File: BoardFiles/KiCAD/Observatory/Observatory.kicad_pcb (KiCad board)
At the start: 4 copper layers, 213.4 x 79.7 mm, 63 parts, among them J1 JScope V+, J10 Dio_Jump, J11 nRF Connections, J12 Sulu Header, J13 Serial, J14 RsTx_Dio, J15 RsRx_Dio, J16 JScope Voltage, J17 WaveGen. 1 Mux Config., J2 Analog Discovery Connection, J20 Mounting Hole, J21 Mounting Hole, J22 Mounting Hole, J23 Mounting Hole, J24 prog. LED, J25 JScope V-, J26 Jumper, J27 Jumper, J28 Jumper, J29 Jumper, J3 Digitial Discovery Connection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, J30 Conn_Coaxial_Small, J31 Jumper, J32 Jumper, J33 Conn_Coaxial_Small, J34 JScope I+, J35 JScope I-, J4 Scope 1 Mux Config., J5 Scope 2 Mux Config., J8 JScope Current IO, J9 5V_in, Q2 2N7002, SW1 SW_DIP_x08, SW2 SW_DIP_x08, U1 1, U2 Scope 1 Mux, U3 Wave Gen. Mux, U4 Scope 2 Mux, U5 Pico

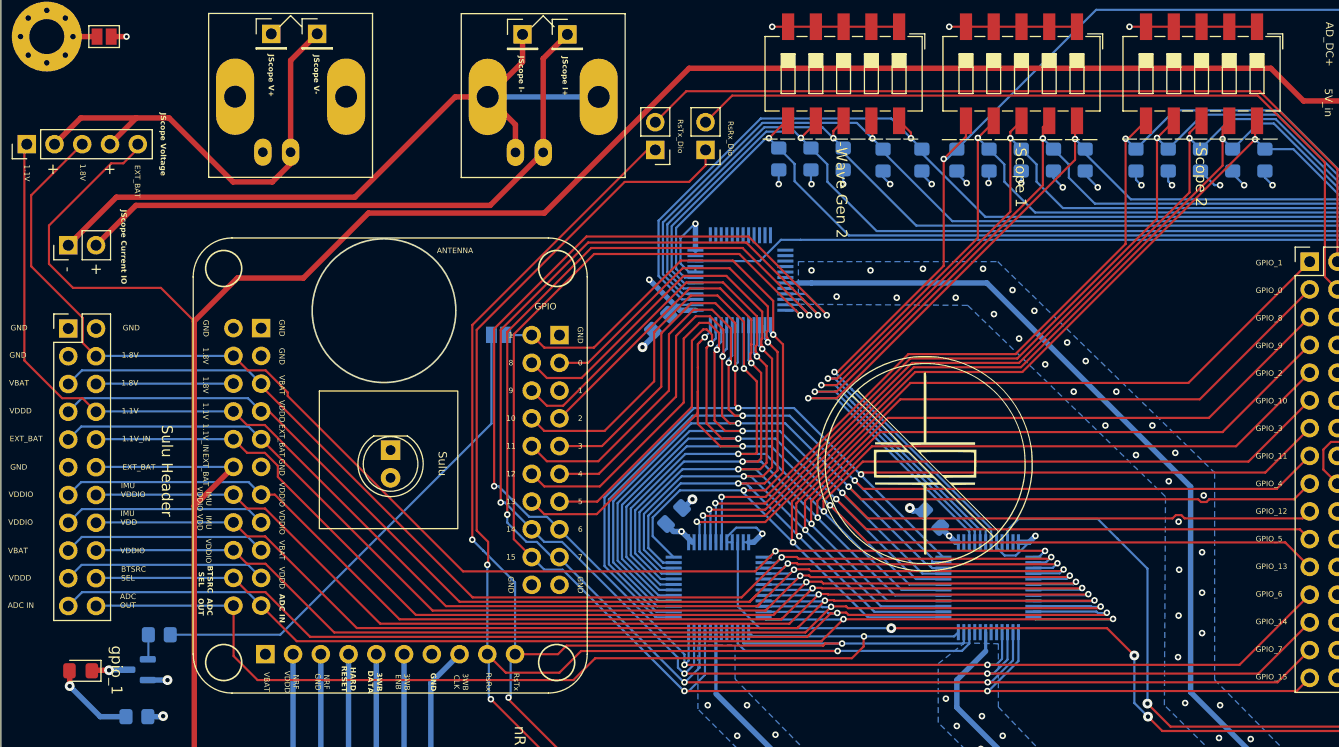
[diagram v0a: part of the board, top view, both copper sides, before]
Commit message: LED circuit fix, added decoupling cap
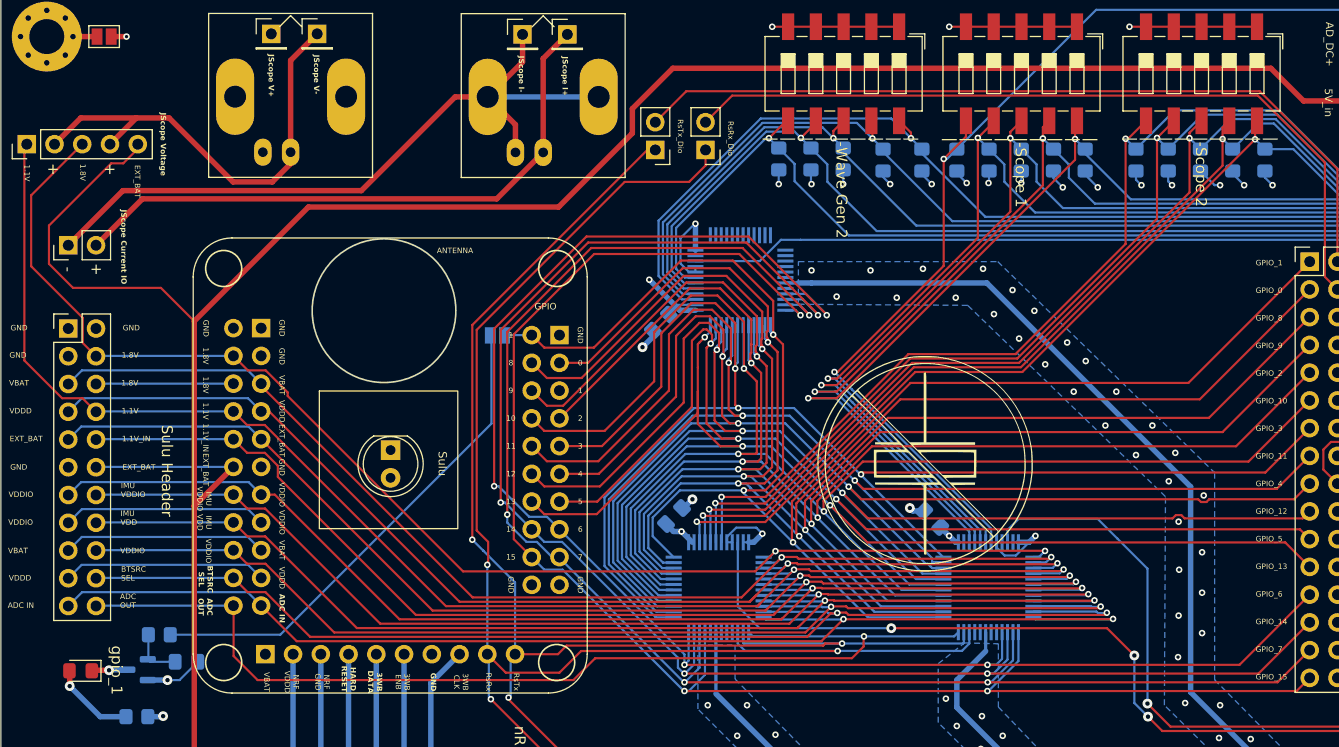
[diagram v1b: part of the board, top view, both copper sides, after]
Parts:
- added C1: 10n, Capacitor_SMD:C_0805_2012Metric_Pad1.18x1.45mm_HandSolder, B.Cu at (58.2, 96.1)
- moved J32 0.11 mm to (86.7, 66.2)
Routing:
- net AD_Scope1-: track 91.8 -> 95.3 mm
- net Net-(Q2-G): track 2.27 -> 4.86 mm
- net Net-(J12-Pin_12): track 209.9 -> 211.2 mm
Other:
- board text added: "WEST LAB CAPSTONE SCUM OBSERVATORY REV2.1"
- board text removed: "WEST LAB CAPSTONE SCUM OBSERVATORY REV2"

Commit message: REV3 begin
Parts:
- removed SW1, SW2: SW_DIP_x08, Button_Switch_SMD:SW_DIP_SPSTx08_Slide_6.7x21.88mm_W8.61mm_P2.54mm_LowProfile
- J11: footprint Connector_PinHeader_2.54mm:PinHeader_1x06_P2.54mm_Vertical -> Connector_PinHeader_2.54mm:PinHeader_1x06_P2.54mm_Horizontal
- J12: value Sulu Header -> Sulu J1 Header
- J13, J9: footprint Connector_PinHeader_2.54mm:PinHeader_1x02_P2.54mm_Vertical -> Connector_PinHeader_2.54mm:PinHeader_1x02_P2.54mm_Horizontal
- J16: value JScope Voltage -> JScope V Ref
- J17, J4, J5: moved to B.Cu
- J24: footprint Connector_PinHeader_2.54mm:PinHeader_1x03_P2.54mm_Vertical -> Button_Switch_THT:SW_CK_JS202011CQN_DPDT_Straight
- J3: value Digitial Discovery Connection Center -> Digitial Discovery Connection
- J31: moved to F.Cu
- J8: value JScope Current IO -> JScope I Loop
- moved J14 181.1 mm to (278.4, 85.7)
- moved J15 179.0 mm to (280.4, 88.1)
- moved J22 177.2 mm to (176.7, -50.3)
- moved J28 174.8 mm to (182.8, -52.5)
- moved J17 154.4 mm to (270.6, 68.1)
- moved J2 138.5 mm to (112.3, 116.6), turned to -90 degrees
- moved J5 136.4 mm to (270.6, 53.5)
- moved J4 119.5 mm to (270.6, 38.4)
- moved J23 109.6 mm to (176.7, -42.4)
- moved J29 107.5 mm to (182.8, -49.0), turned to 0 degrees
- moved J31 99.6 mm to (180.3, -58.0)
- moved R2 95.7 mm to (214.0, 127.0)
- moved R3 95.1 mm to (210.0, 127.0)
- moved R4 94.5 mm to (206.0, 127.0)
- moved R5 93.9 mm to (202.0, 127.0)
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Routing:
- net Net-(J12-Pin_12): track 211.2 -> 13.0 mm
- net WaveGen. Mux Control 4: track 185.5 -> 5.84 mm, vias 1 -> 0
- net WaveGen. Mux Control 3: track 183.4 -> 6.72 mm, vias 1 -> 0
- net AD_Scope2+: track 226.3 -> 52.0 mm
- net WaveGen. Mux Control 2: track 180.5 -> 7.59 mm, vias 1 -> 0
- net Scope 2 Mux ~EN: track 153.4 -> 9.80 mm, vias 2 -> 0
- net Scope 1 Mux ~EN: track 178.8 -> 40.5 mm, vias 4 -> 1
- net Scope 2 Mux Control 4: track 168.4 -> 35.6 mm, vias 2 -> 1
- net WaveGen. 1 Mux ~EN: track 125.8 -> 10.4 mm, vias 2 -> 0
- net AD_Scope1+: track 187.9 -> 73.4 mm
- net WaveGen. Mux Control 1: track 178.0 -> 66.7 mm, vias 1 -> 0
- net Scope 2 Mux Control 3: track 151.5 -> 40.4 mm, vias 2 -> 1
- net WaveGen. Mux Control 0: track 173.9 -> 66.9 mm, vias 1 -> 0
- net Scope 2 Mux Control 2: track 148.4 -> 45.0 mm, vias 2 -> 1
- net Scope 1 Mux Control 1: track 132.9 -> 37.3 mm, vias 2 -> 1
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- removed copper zone on B.Cu, net AD_Scope1-
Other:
- board size 213.4 x 79.7 mm -> 182.1 x 80.6 mm
- board text added: "Current"
- board text added: "Observatory Power V+ Select"
- board text added: "On"
- board text added: "Voltage"
- board text removed: "AD0"
- board text removed: "AD1"
- board text removed: "AD10"
- board text removed: "AD11"
- board text removed: "AD12"
- board text removed: "AD13"
- board text removed: "AD14"
- board text removed: "AD15"
- board text removed: "AD2"
- board text removed: "AD3"
- board text removed: "AD4"
- board text removed: "AD5"
- board text removed: "AD6"
- board text removed: "AD7"
- board text removed: "AD8"
- board text removed: "AD9"
- board text removed: "ADio_Jump"
- board text removed: "Observatory V+"
- board text removed: "Observatory V+ Select"
- board text removed: "V_sys to observatory supply"
- board text removed: "WEST LAB CAPSTONE SCUM OBSERVATORY REV2.1"

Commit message: REV3 begin
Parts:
- removed J14: RsTx_Dio, Connector_PinHeader_2.54mm:PinHeader_1x02_P2.54mm_Vertical
- removed J15: RsRx_Dio, Connector_PinHeader_2.54mm:PinHeader_1x02_P2.54mm_Vertical
- J12: value Sulu J1 Header -> Sulu Header
- J16: value JScope V Ref -> JScope Voltage
- J3: value Digitial Discovery Connection -> Digitial Discovery Connection Center
- J8: value JScope I Loop -> JScope Current IO
- moved J22 121.9 mm to (87.1, 32.4)
- moved J23 121.9 mm to (87.1, 40.3)
- moved J28 121.9 mm to (93.2, 30.2)
- moved J29 121.9 mm to (93.2, 33.7)
- moved J31 121.9 mm to (90.7, 24.7)
- moved J16 16.5 mm to (68.5, 62.9), turned to 90 degrees
- moved J11 7.01 mm to (160.2, 135.4)
- moved J13 7.01 mm to (170.0, 135.4)
- moved J9 7.01 mm to (139.0, 135.4)
- moved U5 6.65 mm to (239.4, 112.5)
- moved C5 2.95 mm to (145.0, 70.8)
- moved U3 2.95 mm to (152.3, 66.9)
- moved J25 2.80 mm to (68.1, 97.4)
- moved J1 2.80 mm to (68.1, 93.2)
- moved J30 2.80 mm to (79.0, 75.6)
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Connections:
- J10 pad 2: DD_DIN_0 -> DD_DIN_1
- J10 pad 4: DD_DIN_1 -> DD_DIN_0
- U5 pad 1: unconnected-(U5-GPIO0-Pad1) -> Scope 1 Mux Control 0
- U5 pad 10: Scope 2 Mux ~EN -> Scope 2 Mux Control 2
- U5 pad 11: WaveGen. 1 Mux ~EN -> Scope 2 Mux Control 3
- U5 pad 2: unconnected-(U5-GPIO1-Pad2) -> Scope 1 Mux Control 1
- U5 pad 21: Scope 2 Mux Control 3 -> unconnected-(U5-GPIO16-Pad21)
- U5 pad 22: Scope 2 Mux Control 2 -> unconnected-(U5-GPIO17-Pad22)
- U5 pad 24: Scope 2 Mux Control 1 -> unconnected-(U5-GPIO18-Pad24)
- U5 pad 25: Scope 2 Mux Control 0 -> unconnected-(U5-GPIO19-Pad25)
- U5 pad 26: Scope 1 Mux Control 0 -> unconnected-(U5-GPIO20-Pad26)
- U5 pad 27: Scope 1 Mux Control 1 -> unconnected-(U5-GPIO21-Pad27)
- U5 pad 29: Scope 1 Mux Control 2 -> unconnected-(U5-GPIO22-Pad29)
- U5 pad 31: Scope 1 Mux Control 3 -> unconnected-(U5-GPIO26_ADC0-Pad31)
- U5 pad 32: Scope 1 Mux Control 4 -> unconnected-(U5-GPIO27_ADC1-Pad32)
- U5 pad 4: unconnected-(U5-GPIO2-Pad4) -> Scope 1 Mux Control 2
- U5 pad 5: unconnected-(U5-GPIO3-Pad5) -> Scope 1 Mux Control 3
- U5 pad 6: unconnected-(U5-GPIO4-Pad6) -> Scope 1 Mux Control 4
- U5 pad 7: unconnected-(U5-GPIO5-Pad7) -> Scope 2 Mux Control 0
- U5 pad 9: Scope 1 Mux ~EN -> Scope 2 Mux Control 1
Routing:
- net Scope 1 Mux Control 0: track 37.5 -> 152.7 mm, vias 1 -> 2
- net Scope 1 Mux Control 1: track 37.3 -> 151.6 mm, vias 1 -> 2
- net WaveGen. Mux Control 4: track 5.84 -> 116.2 mm
- net Scope 1 Mux Control 2: track 37.0 -> 147.0 mm, vias 1 -> 2
- net WaveGen. Mux Control 3: track 6.72 -> 115.5 mm
- net WaveGen. Mux Control 2: track 7.59 -> 115.8 mm
- net Scope 1 Mux Control 3: track 36.8 -> 144.0 mm, vias 1 -> 2
- net Scope 1 Mux Control 4: track 36.5 -> 137.7 mm, vias 1 -> 2
- net Scope 2 Mux Control 4: track 35.6 -> 128.6 mm, vias 1 -> 2
- net Scope 2 Mux Control 3: track 40.4 -> 130.5 mm, vias 1 -> 2
- net Scope 2 Mux Control 0: track 54.2 -> 144.2 mm, vias 1 -> 2
- net Scope 2 Mux Control 2: track 45.0 -> 133.0 mm, vias 1 -> 2
- net Scope 2 Mux Control 1: track 49.7 -> 135.8 mm, vias 1 -> 2
- net WaveGen. Mux Control 1: track 66.7 -> 114.2 mm
- net WaveGen. Mux Control 0: track 66.9 -> 111.4 mm
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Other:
- board size 182.1 x 80.6 mm -> 185.8 x 81.8 mm

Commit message: REV3 DRC pass
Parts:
- removed C1: 10n, Capacitor_SMD:C_0805_2012Metric_Pad1.18x1.45mm_HandSolder
- removed C3, C4: C, Capacitor_SMD:C_0805_2012Metric_Pad1.18x1.45mm_HandSolder
- removed D2: LED, LED_SMD:LED_0805_2012Metric_Pad1.15x1.40mm_HandSolder
- removed G***: LOGO, 3rdPrty_Footprints:NoCrystal
- removed J17: WaveGen. 1 Mux Config., Button_Switch_SMD:SW_DIP_SPSTx05_Slide_6.7x14.26mm_W8.61mm_P2.54mm_LowProfile
- removed J26, J27, J28, J29: Jumper, Jumper:SolderJumper-2_P1.3mm_Open_Pad1.0x1.5mm
- removed J4: Scope 1 Mux Config., Button_Switch_SMD:SW_DIP_SPSTx05_Slide_6.7x14.26mm_W8.61mm_P2.54mm_LowProfile
- removed J5: Scope 2 Mux Config., Button_Switch_SMD:SW_DIP_SPSTx05_Slide_6.7x14.26mm_W8.61mm_P2.54mm_LowProfile
- removed Q2: 2N7002, Package_TO_SOT_SMD:SOT-23
- removed R10, R11, R12, R13, R14, R15, R16, R2, R3, R4, R5, R6, R7, R8, R9: R_up, Resistor_SMD:R_0805_2012Metric_Pad1.20x1.40mm_HandSolder
- removed R19, R20: R, Resistor_SMD:R_0805_2012Metric_Pad1.20x1.40mm_HandSolder
- removed U2: Scope 1 Mux, 3rdPrty_Footprints:SU_48_ADI
- removed U3: Wave Gen. Mux, 3rdPrty_Footprints:SU_48_ADI
- removed U4: Scope 2 Mux, 3rdPrty_Footprints:SU_48_ADI
- added C6: C, Capacitor_SMD:C_0805_2012Metric_Pad1.18x1.45mm_HandSolder, B.Cu at (141.8, 98.9)
- added C7: C, Capacitor_SMD:C_0805_2012Metric_Pad1.18x1.45mm_HandSolder, B.Cu at (163.6, 73.1)
- added C8: C, Capacitor_SMD:C_0805_2012Metric_Pad1.18x1.45mm_HandSolder, B.Cu at (141.4, 73.2)
- added C9: C, Capacitor_SMD:C_0805_2012Metric_Pad1.18x1.45mm_HandSolder, B.Cu at (119.3, 71.5)
- added J36: Mounting Hole, MountingHole:MountingHole_3.2mm_M3_Pad_Via, F.Cu at (163.0, 49.0)
- added J37: Mounting Hole, MountingHole:MountingHole_3.2mm_M3_Pad_Via, F.Cu at (163.0, 133.5)
- added U10: CD74HC4067M, Package_SO:SOIC-24W_7.5x15.4mm_P1.27mm, B.Cu at (172.8, 71.2)
- added U6: CD74HC4067M, Package_SO:SOIC-24W_7.5x15.4mm_P1.27mm, B.Cu at (128.4, 71.2)
- added U7: CD74HC4067M, Package_SO:SOIC-24W_7.5x15.4mm_P1.27mm, B.Cu at (127.9, 96.8)
- added U8: CD74HC4067M, Package_SO:SOIC-24W_7.5x15.4mm_P1.27mm, B.Cu at (150.6, 71.2)
- added U9: CD74HC4067M, Package_SO:SOIC-24W_7.5x15.4mm_P1.27mm, B.Cu at (151.1, 96.8)
- J11: footprint Connector_PinHeader_2.54mm:PinHeader_1x06_P2.54mm_Horizontal -> Connector_PinHeader_2.54mm:PinHeader_1x06_P2.54mm_Vertical
- J13, J9: footprint Connector_PinHeader_2.54mm:PinHeader_1x02_P2.54mm_Horizontal -> Connector_PinHeader_2.54mm:PinHeader_1x02_P2.54mm_Vertical
- J24: value prog. LED -> Observatory PWR
- J31: moved to B.Cu
- J32: footprint Jumper:SolderJumper-2_P1.3mm_Open_Pad1.0x1.5mm -> Jumper:SolderJumper-2_P1.3mm_Bridged_RoundedPad1.0x1.5mm
- moved J23 190.8 mm to (253.5, 133.5)
- moved J31 180.9 mm to (253.5, 103.6), turned to -90 degrees
- moved J22 167.3 mm to (253.5, 49.0)
- moved J2 135.1 mm to (237.0, 64.5), turned to 0 degrees
- moved J24 116.3 mm to (128.6, 121.2)
- moved R18 116.1 mm to (138.5, 117.7)
- moved D1 115.9 mm to (138.5, 123.0), turned to 90 degrees
- moved J16 69.4 mm to (111.8, 117.1), turned to 180 degrees
- moved J34 63.8 mm to (82.2, 135.6), turned to 180 degrees
- moved J35 60.9 mm to (86.3, 135.6), turned to 180 degrees
- moved J1 54.3 mm to (102.1, 135.6), turned to 180 degrees
- moved J25 54.0 mm to (106.3, 135.6), turned to 180 degrees
- moved J3 53.3 mm to (209.4, 63.3), turned to 0 degrees
- moved J8 52.0 mm to (73.8, 113.0), turned to 180 degrees
- moved J30 49.5 mm to (84.4, 124.8), turned to 180 degrees
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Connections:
- J10 pad 13: Scope 1 Mux  12 -> Scope 1 Mux  7
- J10 pad 15: Scope 1 Mux  11 -> Scope 1 Mux  8
- J10 pad 17: Scope 1 Mux  10 -> Scope 1 Mux  9
- J10 pad 19: Scope 1 Mux  9 -> Scope 1 Mux  10
- J10 pad 21: Scope 1 Mux  8 -> Scope 1 Mux  11
- J10 pad 23: Scope 1 Mux  7 -> Scope 1 Mux  12
- J12 pad 10: Scope 1 Mux  22 -> Net-(J12-Pin_10)
- J12 pad 12: Net-(J12-Pin_12) -> +5V
- J12 pad 13: Scope 1 Mux  23 -> Net-(J12-Pin_13)
- J12 pad 16: Scope 1 Mux  25 -> Scope 1 Mux  23
- J12 pad 17: Net-(J12-Pin_17) -> Scope 1 Mux  21
- J12 pad 18: Scope 1 Mux  26 -> Scope 1 Mux  22
- J12 pad 19: Net-(J12-Pin_19) -> Scope 1 Mux  19
- J12 pad 20: Scope 1 Mux  27 -> Scope 1 Mux  20
- J12 pad 21: Scope 1 Mux  28 -> Scope 1 Mux  17
- J12 pad 22: Scope 1 Mux  29 -> Scope 1 Mux  18
- J12 pad 4: Scope 1 Mux  17 -> Net-(J12-Pin_4)
- J12 pad 5: Scope 1 Mux  18 -> Net-(J12-Pin_5)
- J12 pad 6: Net-(J12-Pin_6) -> Scope 1 Mux  29
- J12 pad 7: Scope 1 Mux  19 -> Scope 1 Mux  27
- J12 pad 8: Scope 1 Mux  20 -> Scope 1 Mux  28
- J12 pad 9: Scope 1 Mux  21 -> +5V
- J16 pad 1: Scope 1 Mux  20 -> Scope 1 Mux  28
- J16 pad 3: Scope 1 Mux  17 -> Net-(J12-Pin_4)
- J16 pad 5: Net-(J12-Pin_12) -> +5V
- J20 pad 1: Net-(J20-Pin_1) -> AD_Scope1-
- J21 pad 1: Net-(J21-Pin_1) -> AD_Scope1-
- J22 pad 1: Net-(J22-Pin_1) -> AD_Scope1-
- J23 pad 1: Net-(J23-Pin_1) -> AD_Scope1-
- J24 pad 1: AD_DC_Supply+ -> Net-(J24-Pin_1)
- J24 pad 3: Net-(J12-Pin_12) -> AD_DC_Supply+
- J32 pad 1: Net-(J32-Pin_1) -> +5V
- J32 pad 2: Scope 1 Mux  1 -> Scope 1 Mux  26
- J9 pad 2: Net-(J12-Pin_12) -> Net-(J24-Pin_1)
- U1 pad 10a: Scope 1 Mux  11 -> Scope 1 Mux  8
- U1 pad 10c: Scope 1 Mux  22 -> Net-(J12-Pin_10)
- U1 pad 11a: Scope 1 Mux  10 -> Scope 1 Mux  9
- U1 pad 12a: Scope 1 Mux  9 -> Scope 1 Mux  10
- U1 pad 12c: Net-(J12-Pin_12) -> +5V
- U1 pad 13a: Scope 1 Mux  8 -> Scope 1 Mux  11
- U1 pad 13c: Scope 1 Mux  23 -> Net-(J12-Pin_13)
- U1 pad 14a: Scope 1 Mux  7 -> Scope 1 Mux  12
- U1 pad 16c: Scope 1 Mux  25 -> Scope 1 Mux  23
- U1 pad 17c: Net-(J12-Pin_17) -> Scope 1 Mux  21
- U1 pad 18c: Scope 1 Mux  26 -> Scope 1 Mux  22
- U1 pad 19c: Net-(J12-Pin_19) -> Scope 1 Mux  19
- U1 pad 20c: Scope 1 Mux  27 -> Scope 1 Mux  20
- U1 pad 21c: Scope 1 Mux  28 -> Scope 1 Mux  17
- U1 pad 22c: Scope 1 Mux  29 -> Scope 1 Mux  18
- U1 pad 4c: Scope 1 Mux  17 -> Net-(J12-Pin_4)
- U1 pad 5c: Scope 1 Mux  18 -> Net-(J12-Pin_5)
- U1 pad 6c: Net-(J12-Pin_6) -> Scope 1 Mux  29
- U1 pad 7c: Scope 1 Mux  19 -> Scope 1 Mux  27
- U1 pad 8c: Scope 1 Mux  20 -> Scope 1 Mux  28
- U1 pad 9a: Scope 1 Mux  12 -> Scope 1 Mux  7
- U1 pad 9c: Scope 1 Mux  21 -> +5V
- U5 pad 1: Scope 1 Mux Control 0 -> unconnected-(U5-GPIO0-Pad1)
- U5 pad 10: Scope 2 Mux Control 2 -> Scope 2 Mux ~EN_B
- U5 pad 11: Scope 2 Mux Control 3 -> Scope 1 Mux ~EN_B
- U5 pad 12: Scope 2 Mux Control 4 -> unconnected-(U5-GPIO9-Pad12)
- U5 pad 14: WaveGen. Mux Control 4 -> unconnected-(U5-GPIO10-Pad14)
- U5 pad 15: WaveGen. Mux Control 3 -> unconnected-(U5-GPIO11-Pad15)
- U5 pad 16: WaveGen. Mux Control 2 -> unconnected-(U5-GPIO12-Pad16)
- U5 pad 17: WaveGen. Mux Control 1 -> unconnected-(U5-GPIO13-Pad17)
- U5 pad 19: WaveGen. Mux Control 0 -> unconnected-(U5-GPIO14-Pad19)
- U5 pad 2: Scope 1 Mux Control 1 -> unconnected-(U5-GPIO1-Pad2)
- U5 pad 21: unconnected-(U5-GPIO16-Pad21) -> Scope 2 Mux Control 0
- U5 pad 22: unconnected-(U5-GPIO17-Pad22) -> Scope 2 Mux Control 1
- U5 pad 24: unconnected-(U5-GPIO18-Pad24) -> Scope 1 Mux Control 0
- U5 pad 25: unconnected-(U5-GPIO19-Pad25) -> Scope 1 Mux Control 1
- U5 pad 26: unconnected-(U5-GPIO20-Pad26) -> WaveGen. Mux Control 1
- U5 pad 27: unconnected-(U5-GPIO21-Pad27) -> WaveGen. Mux Control 0
- U5 pad 29: unconnected-(U5-GPIO22-Pad29) -> WaveGen. Mux Control 3
- U5 pad 31: unconnected-(U5-GPIO26_ADC0-Pad31) -> WaveGen. Mux Control 2
- U5 pad 32: unconnected-(U5-GPIO27_ADC1-Pad32) -> WaveGen. 1 Mux ~EN
- U5 pad 34: unconnected-(U5-GPIO28_ADC2-Pad34) -> Scope 1 Mux Control 3
- U5 pad 5: Scope 1 Mux Control 3 -> Scope 1 Mux ~EN_A
- U5 pad 6: Scope 1 Mux Control 4 -> Scope 2 Mux Control 3
- U5 pad 7: Scope 2 Mux Control 0 -> Scope 2 Mux Control 2
- U5 pad 9: Scope 2 Mux Control 1 -> Scope 2 Mux ~EN_A
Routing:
- net AD_WaveGen2: track 152.4 -> 0.00 mm
- net Scope 1 Mux ~EN_A: track 0.00 -> 148.3 mm, vias 0 -> 2
- net Scope 1 Mux Control 4: track 137.7 -> 0.00 mm, vias 2 -> 0
- net AD_DC_Supply+: track 0.00 -> 133.6 mm
- net Scope 2 Mux Control 4: track 128.6 -> 0.00 mm, vias 2 -> 0
- net Scope 2 Mux ~EN_A: track 0.00 -> 116.7 mm, vias 0 -> 2
- net WaveGen. Mux Control 4: track 116.2 -> 0.00 mm
- net Scope 1 Mux ~EN_B: track 0.00 -> 115.4 mm
- net AD_Scope1+: track 71.9 -> 180.8 mm
- net AD_Scope2+: track 54.1 -> 157.5 mm
- net AD_WaveGen1: track 0.00 -> 91.8 mm
- net Scope 2 Mux ~EN_B: track 0.00 -> 90.7 mm
- net WaveGen. 1 Mux ~EN: track 10.4 -> 91.8 mm
- net Scope 1 Mux  25: track 107.9 -> 29.0 mm
- net Net-(J11-Pin_2): track 0.00 -> 74.5 mm
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- added copper zone on In2.Cu, net +5V
- added copper zone on In1.Cu, net AD_Scope1-
- removed copper zone on In1.Cu, net +5V
- removed copper zone on In2.Cu, net AD_Scope1-
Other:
- board size 185.8 x 81.8 mm -> 189.7 x 93.4 mm
- board text removed: "gpio_1"
- board text removed: "| | | | |-Scope 1 | | | |"
- board text removed: "| | | | |-Scope 2 | | | |"
- board text removed: "| | | | |-Wave Gen 2 | | | |"

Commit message: REV3 complete
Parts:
- added G***: LOGO, 3rdPrty_Footprints:NoCrystal, F.Cu at (149.0, 83.7)
- added J4: GPIO Expand, Connector_PinHeader_2.54mm:PinHeader_2x10_P2.54mm_Vertical, F.Cu at (80.8, 54.5)
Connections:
- U1 pad 5a: unconnected-(U1-GPIO1-Pad5a) -> Net-(J4-Pin_5)
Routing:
- net Scope 1 Mux  1: track 159.1 -> 180.1 mm
- net Scope 1 Mux  16: track 151.7 -> 171.5 mm
- net Scope 1 Mux  14: track 143.1 -> 162.9 mm
- net Scope 1 Mux  6: track 127.9 -> 147.6 mm
- net Scope 1 Mux  3: track 147.7 -> 167.4 mm
- net Scope 1 Mux  10: track 125.9 -> 145.5 mm
- net Scope 1 Mux  8: track 117.7 -> 137.3 mm
- net Scope 1 Mux  4: track 138.6 -> 158.2 mm
- net Scope 1 Mux  12: track 134.3 -> 153.9 mm
- net Scope 1 Mux  7: track 122.2 -> 135.8 mm
- net Scope 1 Mux  2: track 147.4 -> 161.0 mm
- net Scope 1 Mux  13: track 132.9 -> 146.5 mm
- net Net-(J4-Pin_5): track 0.00 -> 13.6 mm
- net Scope 1 Mux  11: track 124.5 -> 138.1 mm
- net Scope 1 Mux  9: track 116.1 -> 129.7 mm
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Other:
- board text added: "<-TOP"
- board text added: "WEST LAB SCuM Observatory REV3"

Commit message: REV3.1 done. Labels fixed, reverse polarity protection added. Layout impoved.
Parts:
- removed J1: JScope V+, Connector_PinHeader_2.54mm:PinHeader_1x01_P2.54mm_Vertical
- removed J25: JScope V-, Connector_PinHeader_2.54mm:PinHeader_1x01_P2.54mm_Vertical
- removed J35: JScope I-, Connector_PinHeader_2.54mm:PinHeader_1x01_P2.54mm_Vertical
- added J5: JScope V, Connector_PinHeader_2.54mm:PinHeader_1x02_P2.54mm_Vertical, F.Cu at (105.8, 135.8)
- added J6: JScope I, Connector_PinHeader_2.54mm:PinHeader_1x02_P2.54mm_Vertical, F.Cu at (85.5, 135.7)
- added R19: R_st, Resistor_SMD:R_0805_2012Metric_Pad1.20x1.40mm_HandSolder, B.Cu at (118.1, 122.8)
- added U2: LM66100DCKR, 3rdPrty_Footprints:LM66100DCKR, B.Cu at (118.1, 127.5)
- J34: value JScope I+ -> Jumper; footprint Connector_PinHeader_2.54mm:PinHeader_1x01_P2.54mm_Vertical -> Jumper:SolderJumper-2_P1.3mm_Open_Pad1.0x1.5mm; moved to B.Cu
- moved J8 46.2 mm to (120.0, 113.2)
- moved J34 40.5 mm to (121.8, 127.6), turned to -90 degrees
- moved D1 32.2 mm to (170.7, 123.8)
- moved J24 32.2 mm to (160.8, 122.0)
- moved R18 32.2 mm to (170.7, 118.5)
- moved J16 21.3 mm to (132.8, 120.7)
- moved J11 5.18 mm to (142.3, 133.5)
- moved J13 5.18 mm to (151.0, 133.5)
- moved J9 5.18 mm to (122.9, 133.5)
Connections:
- J34 pad 1: JS_I+ -> Net-(J24-Pin_1)
- J9 pad 2: Net-(J24-Pin_1) -> Net-(J34-Pin_2)
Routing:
- net AD_DC_Supply+: track 133.6 -> 101.7 mm
- net Net-(J24-Pin_1): track 22.0 -> 50.6 mm
- net Net-(J12-Pin_4): track 47.4 -> 71.7 mm, vias 0 -> 1
- net Scope 1 Mux  28: track 115.9 -> 138.1 mm, vias 2 -> 4
- net JS_I-: track 43.3 -> 65.5 mm, vias 0 -> 1
- net JS_I+: track 35.6 -> 57.6 mm, vias 0 -> 1
- net JS_V+: track 35.0 -> 52.8 mm
- net Scope 1 Mux  30: track 112.3 -> 123.9 mm, vias 3 -> 2
- net Net-(J34-Pin_2): track 0.00 -> 8.15 mm
- net Net-(J11-Pin_3): track 65.2 -> 70.5 mm
- net Net-(J11-Pin_4): track 59.1 -> 63.3 mm
- net Net-(J11-Pin_5): track 55.5 -> 58.7 mm
- net Net-(J11-Pin_1): track 64.4 -> 67.0 mm
- net Net-(U2-ST): track 0.00 -> 2.55 mm
- net Net-(J11-Pin_6): track 51.9 -> 54.2 mm
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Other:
- board text added: "0"
- board text added: "1"
- board text added: "10"
- board text added: "11"
- board text added: "12"
- board text added: "13"
- board text added: "14"
- board text added: "15"
- board text added: "2"
- board text added: "3"
- board text added: "4"
- board text added: "5"
- board text added: "6"
- board text added: "7"
- board text added: "8"
- board text added: "9"
- board text added: "WEST LAB SCuM Observatory REV3.1"
- board text removed: "WEST LAB SCuM Observatory REV3"
